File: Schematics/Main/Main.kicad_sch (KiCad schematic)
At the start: 7 parts, among them SW1 SW_Push, SW2 SW_Push, U1 ESP32-WROOM-32E

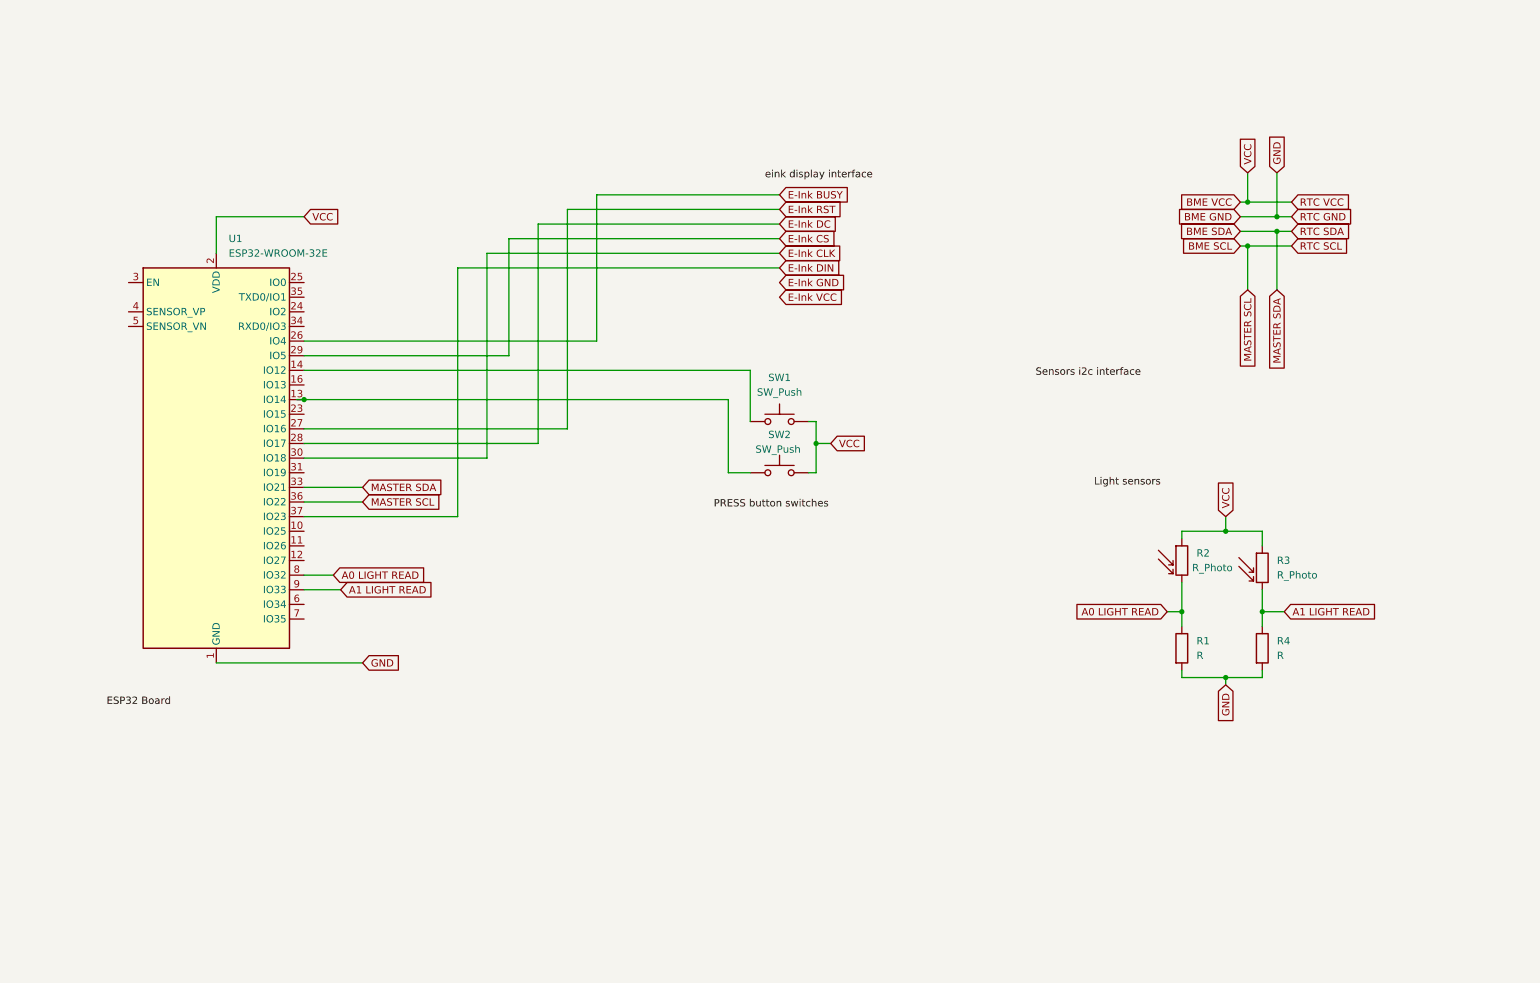
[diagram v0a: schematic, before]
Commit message: seperate pins in code, added buzzer, fixed pinout
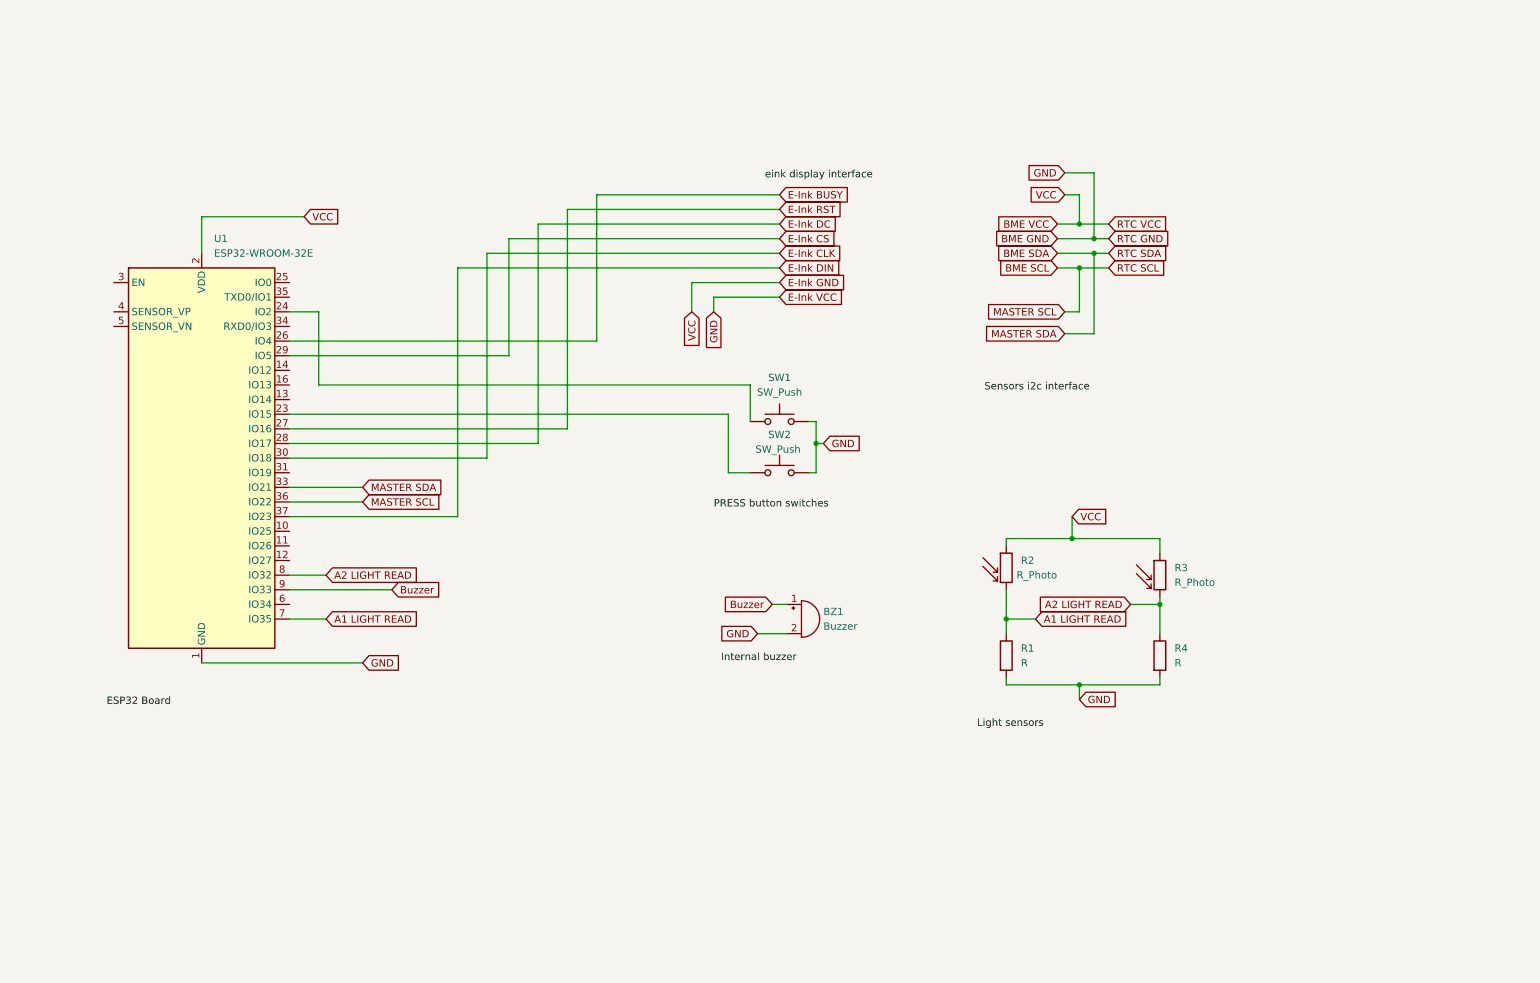
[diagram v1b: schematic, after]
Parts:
- added BZ1: Buzzer, symbol Device:Buzzer
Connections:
- net A1 LIGHT READ: now also R1.1, R2.2, U1.7 (IO35); no longer R3.2, R4.1, U1.9 (IO33)
- net BME GND: now also SW1.2, SW2.2, BZ1.2 (-)
- net BME VCC: no longer SW1.2, SW2.2
- net at SW1.1: now also U1.24 (IO2); no longer U1.14 (IO12)
- net at U1.13 (IO14): no longer SW2.1
- net at U1.23 (IO15): now also SW2.1
- removed net A0 LIGHT READ: R1.1, R2.2, U1.8 (IO32)
- new net A2 LIGHT READ: R3.2, R4.1, U1.8 (IO32)
- new net Buzzer: BZ1.1 (+), U1.9 (IO33)
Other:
- moved on the sheet: R1, R2, R3, R4, U1

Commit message: PCB design and revision 2
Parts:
- removed U1: ESP32-WROOM-32E, RF_Module:ESP32-WROOM-32D, symbol RF_Module:ESP32-WROOM-32E
- added C1: C, Capacitor_THT:C_Radial_D5.0mm_H5.0mm_P2.00mm, symbol Device:C
- added C2: C, Capacitor_THT:C_Disc_D3.0mm_W1.6mm_P2.50mm, symbol Device:C
- added D1, D2: D, Diode_THT:D_DO-41_SOD81_P10.16mm_Horizontal, symbol Device:D
- added H1, H2, H3, H4: MountingHole, MountingHole:MountingHole_4mm, symbol Mechanical:MountingHole
- added J1, J2: Conn_01x19_Socket, Connector_PinHeader_2.54mm:PinHeader_1x19_P2.54mm_Vertical, symbol Connector:Conn_01x19_Socket
- added J3: Conn_01x04_Socket, Connector_PinHeader_2.54mm:PinHeader_1x04_P2.54mm_Vertical, symbol Connector:Conn_01x04_Socket
- added J4: Conn_01x08_Socket, Connector_PinHeader_2.54mm:PinHeader_1x08_P2.54mm_Vertical, symbol Connector:Conn_01x08_Socket
- added J5: Conn_01x06_Pin, Connector_PinHeader_2.54mm:PinHeader_1x06_P2.54mm_Vertical, symbol Connector:Conn_01x06_Pin
- added J6: USB_B_Micro, Connector_USB:USB_Micro-B_Amphenol_10103594-0001LF_Horizontal, symbol Connector:USB_B_Micro
- added SW3: SW_SPST, Connector_PinHeader_2.54mm:PinHeader_1x02_P2.54mm_Vertical, symbol Switch:SW_SPST
- BZ1: footprint (none) -> Buzzer_Beeper:Buzzer_12x9.5RM7.6
- R1, R4: footprint (none) -> Resistor_THT:R_Axial_DIN0207_L6.3mm_D2.5mm_P10.16mm_Horizontal
- R2, R3, SW1, SW2: footprint (none) -> Connector_PinHeader_2.54mm:PinHeader_1x02_P2.54mm_Vertical
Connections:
- net A1 LIGHT READ: now also J2.6 (Pin_6)
- net A2 LIGHT READ: now also J2.7 (Pin_7)
- net BME GND: now also C1.2, C2.2, D2.2 (A), J1.1 (Pin_1), J1.7 (Pin_7), J2.14 (Pin_14), J3.1 (Pin_1), J4.2 (Pin_2), J5.5 (Pin_5)
- net BME SCL: now also J1.3 (Pin_3), J3.4 (Pin_4), J5.3 (Pin_3)
- net BME SDA: now also J1.6 (Pin_6), J3.3 (Pin_3), J5.4 (Pin_4)
- net Buzzer: now also J2.8 (Pin_8)
- net E-Ink BUSY: now also J1.13 (Pin_13), J4.8 (Pin_8)
- net E-Ink CLK: now also J1.9 (Pin_9), J4.4 (Pin_4)
- net E-Ink CS: now also J1.10 (Pin_10), J4.5 (Pin_5)
- net E-Ink DC: now also J1.11 (Pin_11), J4.6 (Pin_6)
- net E-Ink DIN: now also J1.2 (Pin_2), J4.3 (Pin_3)
- net E-Ink RST: now also J1.12 (Pin_12), J4.7 (Pin_7)
- net BTN1: now reaches SW1.1
- net BTN1: now also J1.15 (Pin_15)
- net BTN2: now reaches SW2.1
- net BTN2: now also J1.16 (Pin_16)
- net BME VCC renamed +3.3 V
- net +3.3 V: now also J2.1 (Pin_1), J3.2 (Pin_2), J4.1 (Pin_1), J5.6 (Pin_6)
- new net: J6.1 (VBUS), SW3.1 (A)
- new net: D1.2 (A), SW3.2 (B)
- new net: D2.1 (K), J6.5 (GND)
- new net +5 v: C1.1, C2.1, D1.1 (K), J2.19 (Pin_19)
- new net ESP_EN: J2.2 (Pin_2)
- new net GPI34: J2.5 (Pin_5)
- new net GPI36: J2.3 (Pin_3)
- new net GPI39: J2.4 (Pin_4)
- new net GPIO0: J1.14 (Pin_14)
- new net GPIO1: J1.4 (Pin_4)
- new net GPIO10: J2.17 (Pin_17)
- new net GPIO11: J2.18 (Pin_18)
- new net GPIO12: J2.13 (Pin_13)
- new net GPIO13: J2.15 (Pin_15)
- new net GPIO14: J2.12 (Pin_12)
- new net GPIO19: J1.8 (Pin_8)
- new net GPIO25: J2.9 (Pin_9)
- new net GPIO26: J2.10 (Pin_10)
- new net GPIO27: J2.11 (Pin_11)
- new net GPIO3: J1.5 (Pin_5)
- new net GPIO6: J1.19 (Pin_19)
- new net GPIO7: J1.18 (Pin_18)
- new net GPIO8: J1.17 (Pin_17)
- new net GPIO9: J2.16 (Pin_16)
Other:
- moved on the sheet: BZ1, R1, R2, R3, R4, SW1, SW2
